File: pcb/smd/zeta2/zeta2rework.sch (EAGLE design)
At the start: 114 parts, among them IC1 MAX6520, IC2 L293DD, IC3 L293DD, Q12 8MHz, U1 MPU-6050, U2 INA219, U4 INA219, U5 DS18B20U+

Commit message: added hall effect sensor
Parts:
- added C19, C30, C32, C35, C42, C44: 4.7nF, rcl:C-EUC0603
- added R29, R32, R34: 1.2k, rcl:R-EU_R0603
- added TLE4905L, TLE4905L1, TLE4905L2: JST-PH_3-PIN_HEADER, srg:JST-PH_3-PIN_HEADER
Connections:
- new net HALL_1: C30.2, R29.1, TLE4905L.3
- new net HALL_2: C35.2, R32.1, TLE4905L1.3
- new net HALL_3: C44.2, R34.1, TLE4905L2.3
- net +5V: now also C19.1, C32.1, C42.1, R29.2, R32.2, R34.2, TLE4905L.1, TLE4905L1.1, TLE4905L2.1
- net GND: now also C19.2, C30.1, C32.2, C35.1, C42.2, C44.1, TLE4905L.2, TLE4905L1.2, TLE4905L2.2
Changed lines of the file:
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@@
 <part name="ONE_WIRE" library="srg" deviceset="JST-PH_3-PIN_HEADER" device=""/>
 <part name="SUPPLY_IN1" library="microbuilder" deviceset="TERMBLOCK_1X2" device="-3.5MM"/>
+<part name="TLE4905L" library="srg" deviceset="JST-PH_3-PIN_HEADER" device=""/>
+<part name="P+10" library="supply1" library_urn="urn:adsk.eagle:library:371" deviceset="+5V" device=""/>
+<part name="C19" library="rcl" library_urn="urn:adsk.eagle:library:334" deviceset="C-EU" device="C0603" package3d_urn="urn:adsk.eagle:package:23616/2" value="4.7nF"/>
+<part name="C30" library="rcl" library_urn="urn:adsk.eagle:library:334" deviceset="C-EU" device="C0603" package3d_urn="urn:adsk.eagle:package:23616/2" value="4.7nF"/>
+<part name="R29" library="rcl" library_urn="urn:adsk.eagle:library:334" deviceset="R-EU_" device="R0603" package3d_urn="urn:adsk.eagle:package:23555/2" value="1.2k"/>
+<part name="GND17" library="supply1" library_urn="urn:adsk.eagle:library:371" deviceset="GND" device=""/>
+<part name="TLE4905L1" library="srg" deviceset="JST-PH_3-PIN_HEADER" device=""/>
+<part name="P+17" library="supply1" library_urn="urn:adsk.eagle:library:371" deviceset="+5V" device=""/>
+<part name="C32" library="rcl" library_urn="urn:adsk.eagle:library:334" deviceset="C-EU" device="C0603" package3d_urn="urn:adsk.eagle:package:23616/2" value="4.7nF"/>
+<part name="C35" library="rcl" library_urn="urn:adsk.eagle:library:334" deviceset="C-EU" device="C0603" package3d_urn="urn:adsk.eagle:package:23616/2" value="4.7nF"/>
+<part name="R32" library="rcl" library_urn="urn:adsk.eagle:library:334" deviceset="R-EU_" device="R0603" package3d_urn="urn:adsk.eagle:package:23555/2" value="1.2k"/>
+<part name="GND28" library="supply1" library_urn="urn:adsk.eagle:library:371" deviceset="GND" device=""/>
+<part name="TLE4905L2" library="srg" deviceset="JST-PH_3-PIN_HEADER" device=""/>
+<part name="P+18" library="supply1" library_urn="urn:adsk.eagle:library:371" deviceset="+5V" device=""/>
+<part name="C42" library="rcl" library_urn="urn:adsk.eagle:library:334" deviceset="C-EU" device="C0603" package3d_urn="urn:adsk.eagle:package:23616/2" value="4.7nF"/>
+<part name="C44" library="rcl" library_urn="urn:adsk.eagle:library:334" deviceset="C-EU" device="C0603" package3d_urn="urn:adsk.eagle:package:23616/2" value="4.7nF"/>
+<part name="R34" library="rcl" library_urn="urn:adsk.eagle:library:334" deviceset="R-EU_" device="R0603" package3d_urn="urn:adsk.eagle:package:23555/2" value="1.2k"/>
+<part name="GND31" library="supply1" library_urn="urn:adsk.eagle:library:371" deviceset="GND" device=""/>
 </parts>
 <sheets>
@@
 <instance part="ONE_WIRE" gate="G$1" x="281.94" y="-177.8"/>
 <instance part="SUPPLY_IN1" gate="G$1" x="-88.9" y="40.64" rot="MR180"/>
+<instance part="TLE4905L" gate="G$1" x="353.06" y="12.7"/>
+<instance part="P+10" gate="1" x="327.66" y="27.94"/>
+<instance part="C19" gate="G$1" x="337.82" y="17.78"/>
+<instance part="C30" gate="G$1" x="337.82" y="7.62"/>
+<instance part="R29" gate="G$1" x="327.66" y="12.7" rot="R90"/>
+<instance part="GND17" gate="1" x="332.74" y="7.62"/>
+<instance part="TLE4905L1" gate="G$1" x="353.06" y="-20.32"/>
+<instance part="P+17" gate="1" x="327.66" y="-5.08"/>
+<instance part="C32" gate="G$1" x="337.82" y="-15.24"/>
+<instance part="C35" gate="G$1" x="337.82" y="-25.4"/>
+<instance part="R32" gate="G$1" x="327.66" y="-20.32" rot="R90"/>
+<instance part="GND28" gate="1" x="332.74" y="-25.4"/>
+<instance part="TLE4905L2" gate="G$1" x="353.06" y="-50.8"/>
+<instance part="P+18" gate="1" x="327.66" y="-35.56"/>
+<instance part="C42" gate="G$1" x="337.82" y="-45.72"/>
+<instance part="C44" gate="G$1" x="337.82" y="-55.88"/>
+<instance part="R34" gate="G$1" x="327.66" y="-50.8" rot="R90"/>
+<instance part="GND31" gate="1" x="332.74" y="-55.88"/>
 </instances>
 <busses>
@@
 <junction x="269.24" y="-180.34"/>
 </segment>
+<segment>
+<pinref part="GND17" gate="1" pin="GND"/>
+<pinref part="C19" gate="G$1" pin="2"/>
+<pinref part="C30" gate="G$1" pin="1"/>
+<wire x1="337.82" y1="10.16" x2="337.82" y2="12.7" width="0.1524" layer="91"/>
+<wire x1="332.74" y1="10.16" x2="332.74" y2="12.7" width="0.1524" layer="91"/>
+<wire x1="332.74" y1="12.7" x2="337.82" y2="12.7" width="0.1524" layer="91"/>
+<junction x="337.82" y="12.7"/>
+<pinref part="TLE4905L" gate="G$1" pin="2"/>
+<wire x1="347.98" y1="12.7" x2="337.82" y2="12.7" width="0.1524" layer="91"/>
+</segment>
+<segment>
+<pinref part="GND28" gate="1" pin="GND"/>
+<pinref part="C32" gate="G$1" pin="2"/>
+<pinref part="C35" gate="G$1" pin="1"/>
+<wire x1="337.82" y1="-22.86" x2="337.82" y2="-20.32" width="0.1524" layer="91"/>
+<wire x1="332.74" y1="-22.86" x2="332.74" y2="-20.32" width="0.1524" layer="91"/>
+<wire x1="332.74" y1="-20.32" x2="337.82" y2="-20.32" width="0.1524" layer="91"/>
+<junction x="337.82" y="-20.32"/>
+<pinref part="TLE4905L1" gate="G$1" pin="2"/>
+<wire x1="347.98" y1="-20.32" x2="337.82" y2="-20.32" width="0.1524" layer="91"/>
+</segment>
+<segment>
+<pinref part="GND31" gate="1" pin="GND"/>
+<pinref part="C42" gate="G$1" pin="2"/>
+<pinref part="C44" gate="G$1" pin="1"/>
+<wire x1="337.82" y1="-53.34" x2="337.82" y2="-50.8" width="0.1524" layer="91"/>
+<wire x1="332.74" y1="-53.34" x2="332.74" y2="-50.8" width="0.1524" layer="91"/>
+<wire x1="332.74" y1="-50.8" x2="337.82" y2="-50.8" width="0.1524" layer="91"/>
+<junction x="337.82" y="-50.8"/>
+<pinref part="TLE4905L2" gate="G$1" pin="2"/>
+<wire x1="347.98" y1="-50.8" x2="337.82" y2="-50.8" width="0.1524" layer="91"/>
+</segment>
 </net>
 <net name="V+" class="0">
@@
 <junction x="271.78" y="-96.52"/>
 </segment>
+<segment>
+<pinref part="C19" gate="G$1" pin="1"/>
+<wire x1="337.82" y1="20.32" x2="347.98" y2="20.32" width="0.1524" layer="91"/>
+<pinref part="TLE4905L" gate="G$1" pin="1"/>
+<wire x1="347.98" y1="20.32" x2="347.98" y2="15.24" width="0.1524" layer="91"/>
+<pinref part="R29" gate="G$1" pin="2"/>
+<wire x1="327.66" y1="17.78" x2="327.66" y2="20.32" width="0.1524" layer="91"/>
+<wire x1="327.66" y1="20.32" x2="337.82" y2="20.32" width="0.1524" layer="91"/>
+<junction x="337.82" y="20.32"/>
+<pinref part="P+10" gate="1" pin="+5V"/>
+<wire x1="327.66" y1="20.32" x2="327.66" y2="25.4" width="0.1524" layer="91"/>
+<junction x="327.66" y="20.32"/>
+</segment>
+<segment>
+<pinref part="C32" gate="G$1" pin="1"/>
+<wire x1="337.82" y1="-12.7" x2="347.98" y2="-12.7" width="0.1524" layer="91"/>
+<pinref part="TLE4905L1" gate="G$1" pin="1"/>
+<wire x1="347.98" y1="-12.7" x2="347.98" y2="-17.78" width="0.1524" layer="91"/>
+<pinref part="R32" gate="G$1" pin="2"/>
+<wire x1="327.66" y1="-15.24" x2="327.66" y2="-12.7" width="0.1524" layer="91"/>
+<wire x1="327.66" y1="-12.7" x2="337.82" y2="-12.7" width="0.1524" layer="91"/>
+<junction x="337.82" y="-12.7"/>
+<pinref part="P+17" gate="1" pin="+5V"/>
+<wire x1="327.66" y1="-12.7" x2="327.66" y2="-7.62" width="0.1524" layer="91"/>
+<junction x="327.66" y="-12.7"/>
+</segment>
+<segment>
+<pinref part="C42" gate="G$1" pin="1"/>
+<wire x1="337.82" y1="-43.18" x2="347.98" y2="-43.18" width="0.1524" layer="91"/>
+<pinref part="TLE4905L2" gate="G$1" pin="1"/>
+<wire x1="347.98" y1="-43.18" x2="347.98" y2="-48.26" width="0.1524" layer="91"/>
+<pinref part="R34" gate="G$1" pin="2"/>
+<wire x1="327.66" y1="-45.72" x2="327.66" y2="-43.18" width="0.1524" layer="91"/>
+<wire x1="327.66" y1="-43.18" x2="337.82" y2="-43.18" width="0.1524" layer="91"/>
+<junction x="337.82" y="-43.18"/>
+<pinref part="P+18" gate="1" pin="+5V"/>
+<wire x1="327.66" y1="-43.18" x2="327.66" y2="-38.1" width="0.1524" layer="91"/>
+<junction x="327.66" y="-43.18"/>
+</segment>
 </net>
 <net name="SCL" class="0">
@@
 </segment>
 </net>
+<net name="HALL_1" class="0">
+<segment>
+<label x="314.96" y="2.54" size="1.778" layer="95"/>
+<pinref part="C30" gate="G$1" pin="2"/>
+<wire x1="337.82" y1="2.54" x2="327.66" y2="2.54" width="0.1524" layer="91"/>
+<pinref part="R29" gate="G$1" pin="1"/>
+<wire x1="327.66" y1="2.54" x2="327.66" y2="7.62" width="0.1524" layer="91"/>
+<wire x1="337.82" y1="2.54" x2="347.98" y2="2.54" width="0.1524" layer="91"/>
+<junction x="337.82" y="2.54"/>
+<pinref part="TLE4905L" gate="G$1" pin="3"/>
+<wire x1="347.98" y1="2.54" x2="347.98" y2="10.16" width="0.1524" layer="91"/>
+<wire x1="327.66" y1="2.54" x2="325.12" y2="2.54" width="0.1524" layer="91"/>
+<junction x="327.66" y="2.54"/>
+</segment>
+</net>
+<net name="HALL_2" class="0">
+<segment>
+<label x="314.96" y="-30.48" size="1.778" layer="95"/>
+<pinref part="C35" gate="G$1" pin="2"/>
+<wire x1="337.82" y1="-30.48" x2="327.66" y2="-30.48" width="0.1524" layer="91"/>
+<pinref part="R32" gate="G$1" pin="1"/>
+<wire x1="327.66" y1="-30.48" x2="327.66" y2="-25.4" width="0.1524" layer="91"/>
+<wire x1="337.82" y1="-30.48" x2="347.98" y2="-30.48" width="0.1524" layer="91"/>
+<junction x="337.82" y="-30.48"/>
+<pinref part="TLE4905L1" gate="G$1" pin="3"/>
+<wire x1="347.98" y1="-30.48" x2="347.98" y2="-22.86" width="0.1524" layer="91"/>
+<wire x1="327.66" y1="-30.48" x2="325.12" y2="-30.48" width="0.1524" layer="91"/>
+<junction x="327.66" y="-30.48"/>
+</segment>
+</net>
+<net name="HALL_3" class="0">
+<segment>
+<label x="314.96" y="-60.96" size="1.778" layer="95"/>
+<pinref part="C44" gate="G$1" pin="2"/>
+<wire x1="337.82" y1="-60.96" x2="327.66" y2="-60.96" width="0.1524" layer="91"/>
+<pinref part="R34" gate="G$1" pin="1"/>
+<wire x1="327.66" y1="-60.96" x2="327.66" y2="-55.88" width="0.1524" layer="91"/>
+<wire x1="337.82" y1="-60.96" x2="347.98" y2="-60.96" width="0.1524" layer="91"/>
+<junction x="337.82" y="-60.96"/>
+<pinref part="TLE4905L2" gate="G$1" pin="3"/>
+<wire x1="347.98" y1="-60.96" x2="347.98" y2="-53.34" width="0.1524" layer="91"/>
+<wire x1="327.66" y1="-60.96" x2="325.12" y2="-60.96" width="0.1524" layer="91"/>
+<junction x="327.66" y="-60.96"/>
+</segment>
+</net>

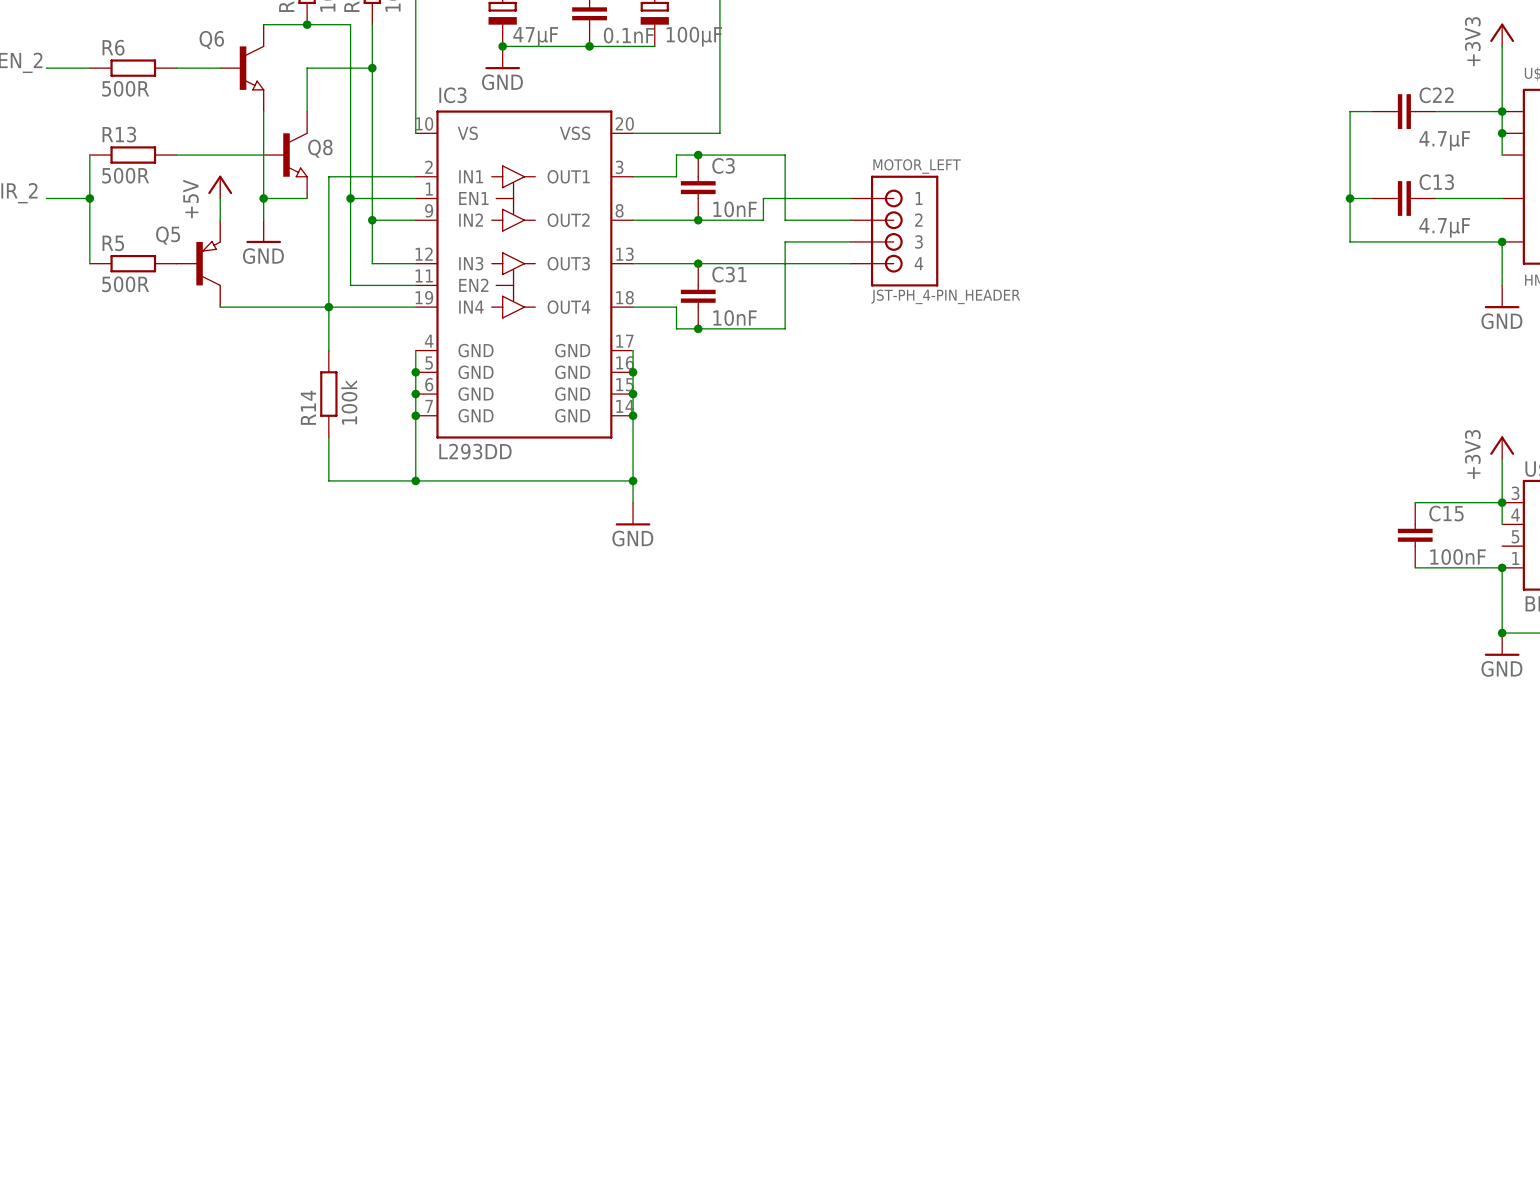
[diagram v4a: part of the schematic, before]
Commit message: adde capicator for mp6500
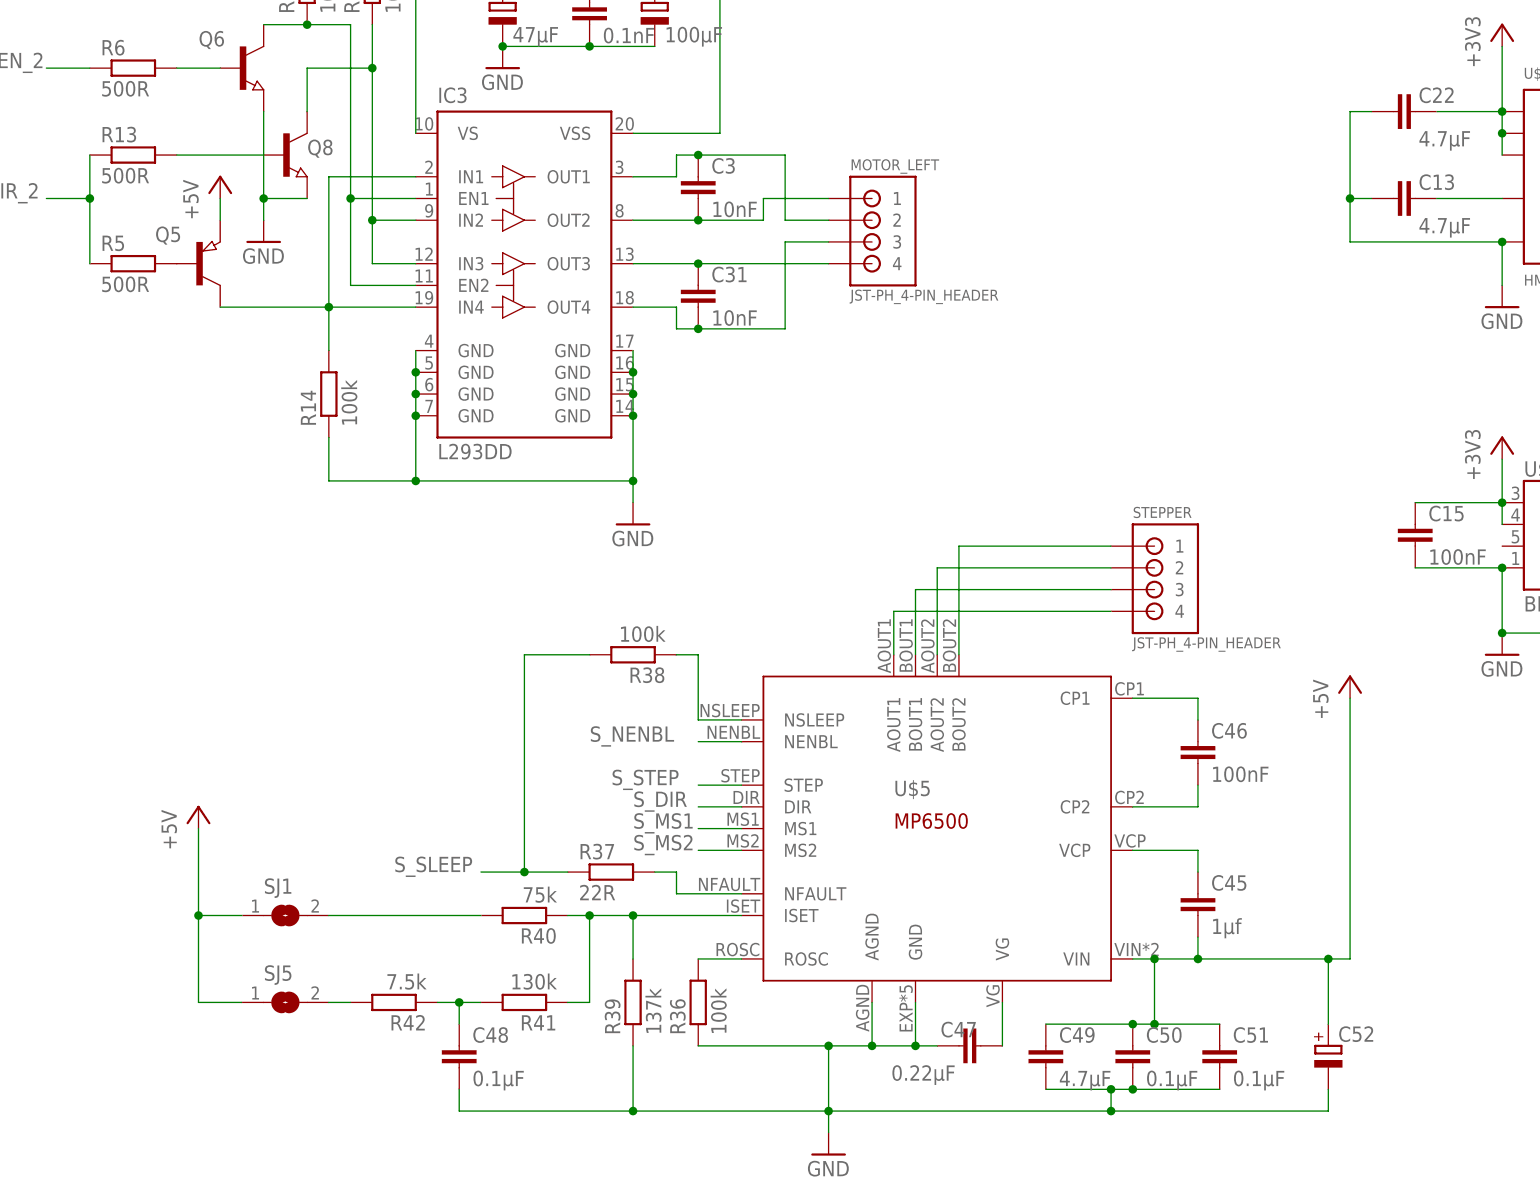
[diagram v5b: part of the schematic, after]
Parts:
- added C45: 1µf, rcl:C-EUC0603
- added C46: 100nF, rcl:C-EUC0603
- added C47: 0.22µF, rcl:C-EUC0603
- added C48, C50, C51: 0.1µF, rcl:C-EUC0603
- added C49: 4.7µF, rcl:C-EUC0603
- added C52: (no value), rcl:CPOL-EU150CLZ-0810
- added R36, R38: 100k, rcl:R-EU_R0603
- added R37: 22R, rcl:R-EU_R0603
- added R39: 137k, rcl:R-EU_R0603
- added R40: 75k, rcl:R-EU_R0603
- added R41: 130k, rcl:R-EU_R0603
- added R42: 7.5k, rcl:R-EU_R0603
- added SJ1, SJ5: (no value), microbuilder:SOLDERJUMPERREFLOW_NOPASTE
- added STEPPER: JST-PH_4-PIN_HEADER, srg:JST-PH_4-PIN_HEADER
- added U$5: MP6500, mp6500:MP6500
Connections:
- new net N$51: C45.1, U$5.VCP
- new net N$52: R38.1, U$5.NSLEEP
- new net N$53: C46.2, U$5.CP2
- new net N$54: C46.1, U$5.CP1
- new net N$57: C47.2, U$5.VG
- new net N$58: R36.2, U$5.ROSC
- new net N$59: R37.2, U$5.NFAULT
- new net N$61: STEPPER.1, U$5.BOUT2
- new net N$62: STEPPER.2, U$5.AOUT2
- new net N$63: R39.2, R40.1, R41.1, U$5.ISET
- new net N$64: STEPPER.3, U$5.BOUT1
- new net N$65: R40.2, SJ1.2
- new net N$66: R42.2, SJ5.2
- new net N$67: C48.1, R41.2, R42.1
- new net N$68: STEPPER.4, U$5.AOUT1
- new net S_MS1: U$5.MS1
- new net S_MS2: U$5.MS2
- new net S_NENBL: U$5.NENBL
- new net S_SLEEP: R37.1, R38.2
- new net S_STEP: U$5.STEP
- net +5V: now also C45.2, C49.1, C50.1, C51.1, C52.+, SJ1.1, SJ5.1, U$5.VIN
- net GND: now also C47.1, C48.2, C49.2, C50.2, C51.2, C52.-, R36.1, R39.1, U$5.AGND, U$5.GND
- net S_DIR: now also U$5.DIR
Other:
- moved on the sheet: MOTOR_LEFT
